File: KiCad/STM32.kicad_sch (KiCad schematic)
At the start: 33 parts, among them J2 Debug, J3 USB_C_Receptacle_USB2.0_16P, SW1 BOOT, SW2 RESET, U1 STM32H743VIT6, U4 W25Q64, Y1 25Mhz

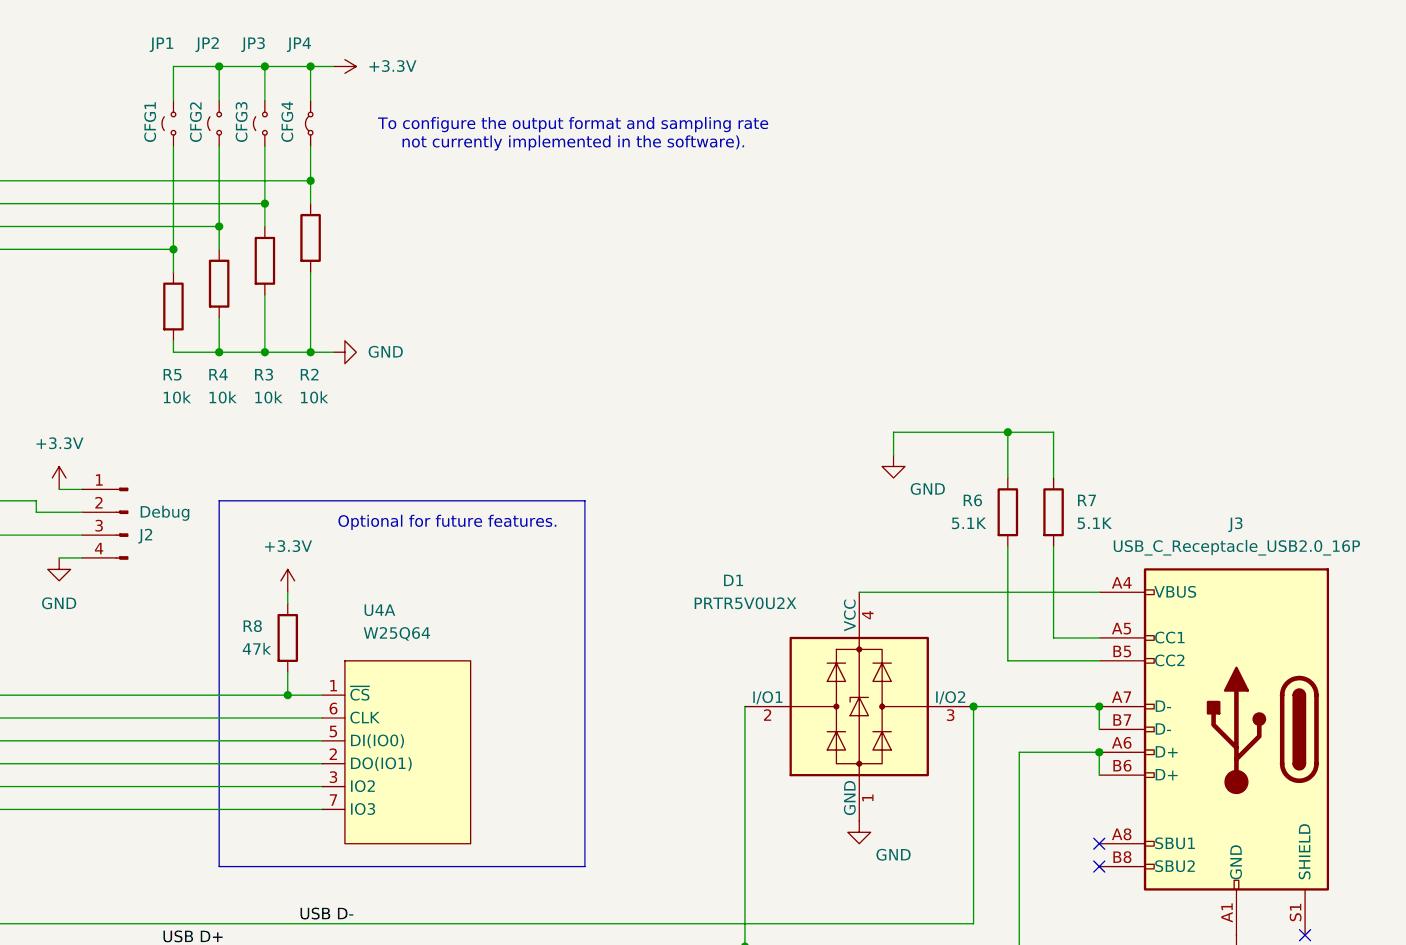
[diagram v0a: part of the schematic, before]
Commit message: Minor and non-functional changes migration to KiCad 9
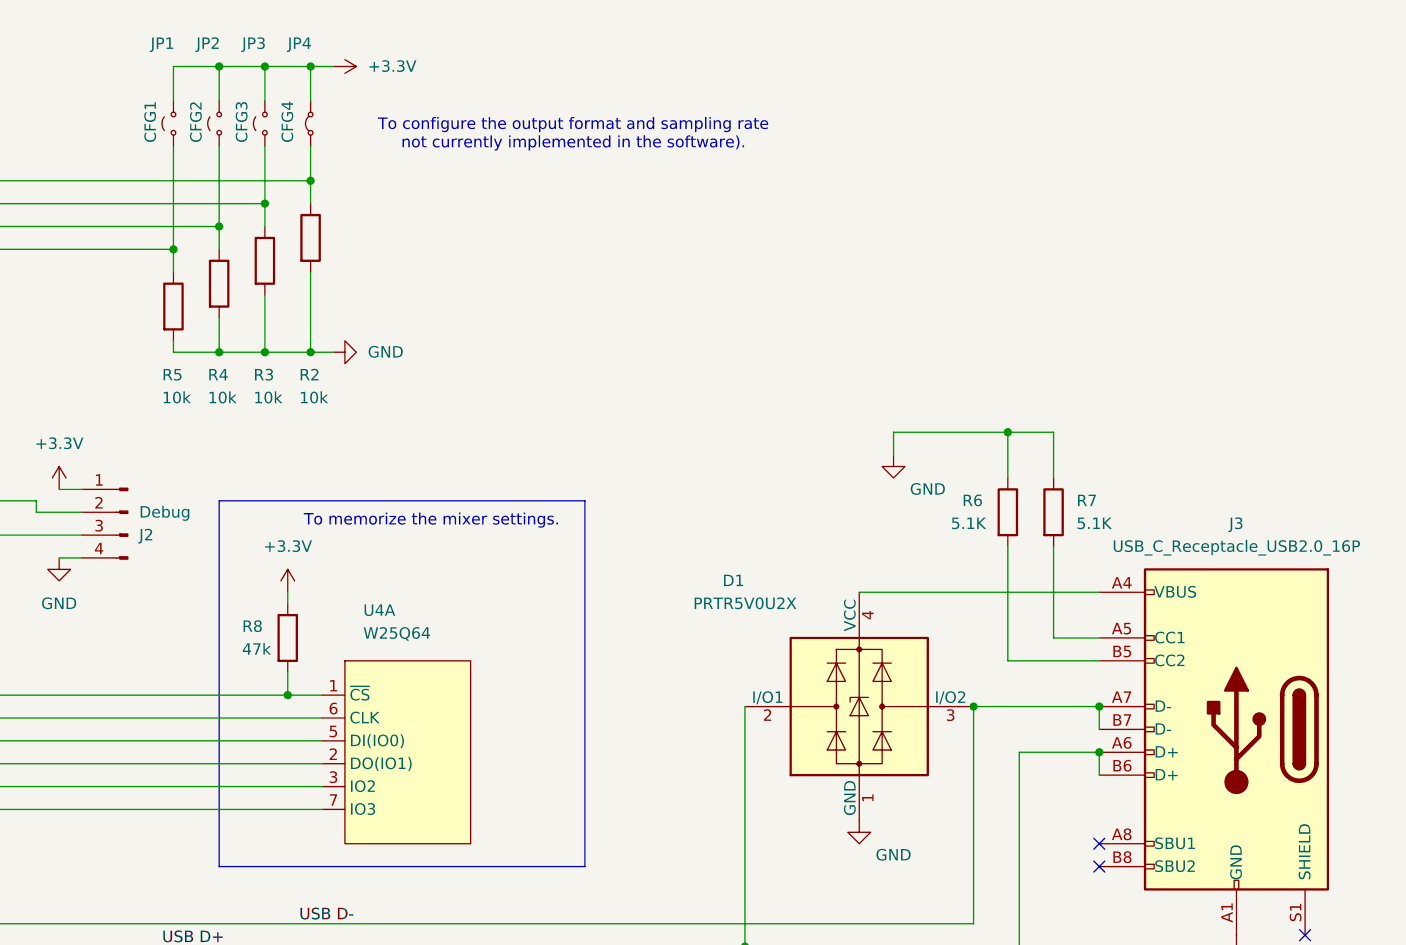
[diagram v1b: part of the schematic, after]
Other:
- note added: "To memorize the mixer settings."
- note removed: "Optional for future features."
